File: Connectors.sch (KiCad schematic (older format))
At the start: 1 part, among them J1 USB

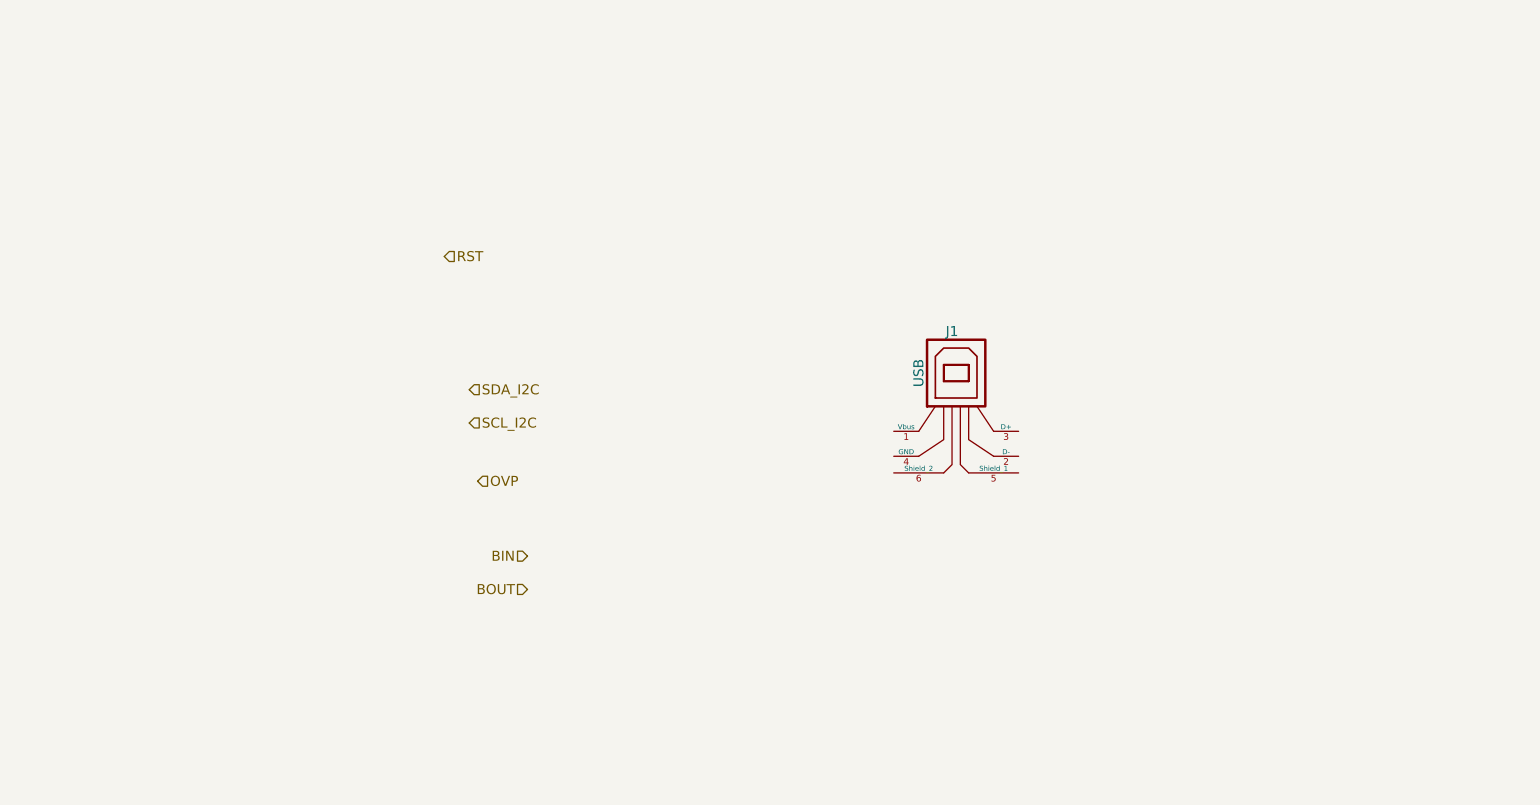
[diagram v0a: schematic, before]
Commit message: Started placing components
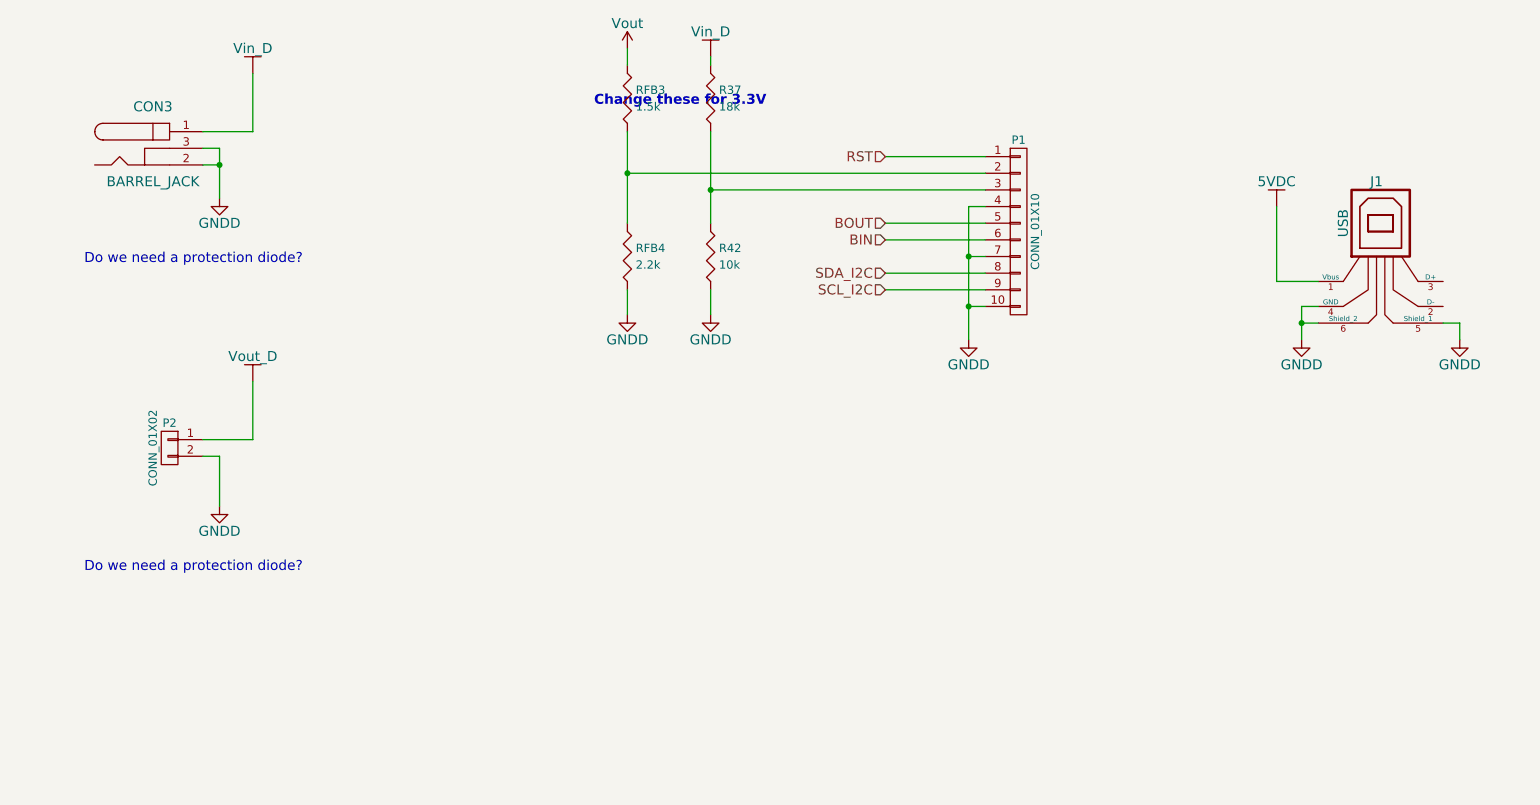
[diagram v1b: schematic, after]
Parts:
- added CON3: BARREL_JACK, Connect:BARREL_JACK, symbol BARREL_JACK
- added P1: CONN_01X10, Socket_Strips:Socket_Strip_Straight_1x10, symbol CONN_01X10
- added P2: CONN_01X02, Socket_Strips:Socket_Strip_Straight_1x02, symbol CONN_01X02
- added R37: 18k, Resistors_SMD:R_0805_HandSoldering, symbol Rv
- added R42: 10k, Resistors_SMD:R_0805_HandSoldering, symbol Rv
- added RFB3: 1.5k, Resistors_SMD:R_0805_HandSoldering, symbol Rv
- added RFB4: 2.2k, Resistors_SMD:R_0805_HandSoldering, symbol Rv
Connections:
- net BIN: now also P1.6 (P6)
- net BOUT: now also P1.5 (P5)
- net RST: now also P1.1 (P1)
- net SCL_I2C: now also P1.9 (P9)
- net SDA_I2C: now also P1.8 (P8)
- net 5VDC: now reaches J1.1 (Vbus)
- net GNDD: now reaches J1.4 (GND)
- net GNDD: now also J1.5 (Shield_1), J1.6 (Shield_2), CON3.2, CON3.3, P1.10 (P10), P1.4 (P4), P1.7 (P7), P2.2 (P2), R42.2, RFB4.2
- new net: P1.3 (P3), R37.2, R42.1
- new net: P1.2 (P2), RFB3.2, RFB4.1
- new net Vin_D: CON3.1, R37.1
- new net Vout: RFB3.1
- new net Vout_D: P2.1 (P1)
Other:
- note added: "Change these for 3.3V"
- note added: "Do we need a protection diode?\n"
- moved on the sheet: J1

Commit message: still trying to get initial placements done.  Still need to fine-tune
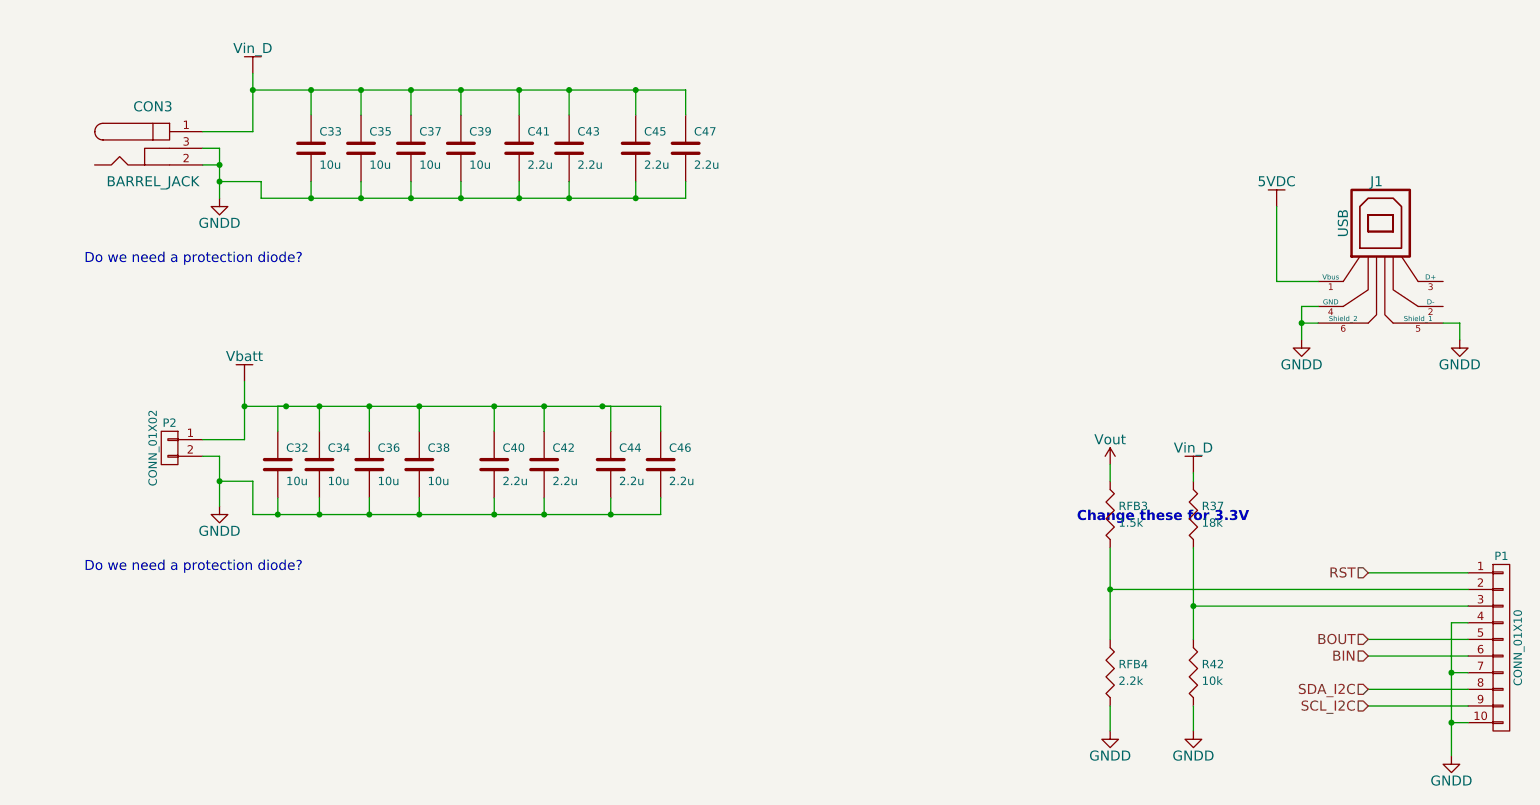
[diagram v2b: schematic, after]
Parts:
- added C32, C33, C34, C35, C36, C37, C38, C39: 10u, Capacitors_SMD:C_0603_HandSoldering, symbol C
- added C40, C41, C42, C43, C44, C45, C46, C47: 2.2u, Capacitors_SMD:C_0603_HandSoldering, symbol C
- R37, R42, RFB3, RFB4: footprint Resistors_SMD:R_0805_HandSoldering -> Resistors_SMD:R_0603_HandSoldering
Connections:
- net GNDD: now also C32.2, C33.2, C34.2, C35.2, C36.2, C37.2, C38.2, C39.2, C40.2, C41.2, C42.2, C43.2, C44.2, C45.2, C46.2, C47.2
- net Vin_D: now also C33.1, C35.1, C37.1, C39.1, C41.1, C43.1, C45.1, C47.1
- net Vout_D renamed Vbatt
- net Vbatt: now also C32.1, C34.1, C36.1, C38.1, C40.1, C42.1, C44.1, C46.1
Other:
- moved on the sheet: P1, R37, R42, RFB3, RFB4

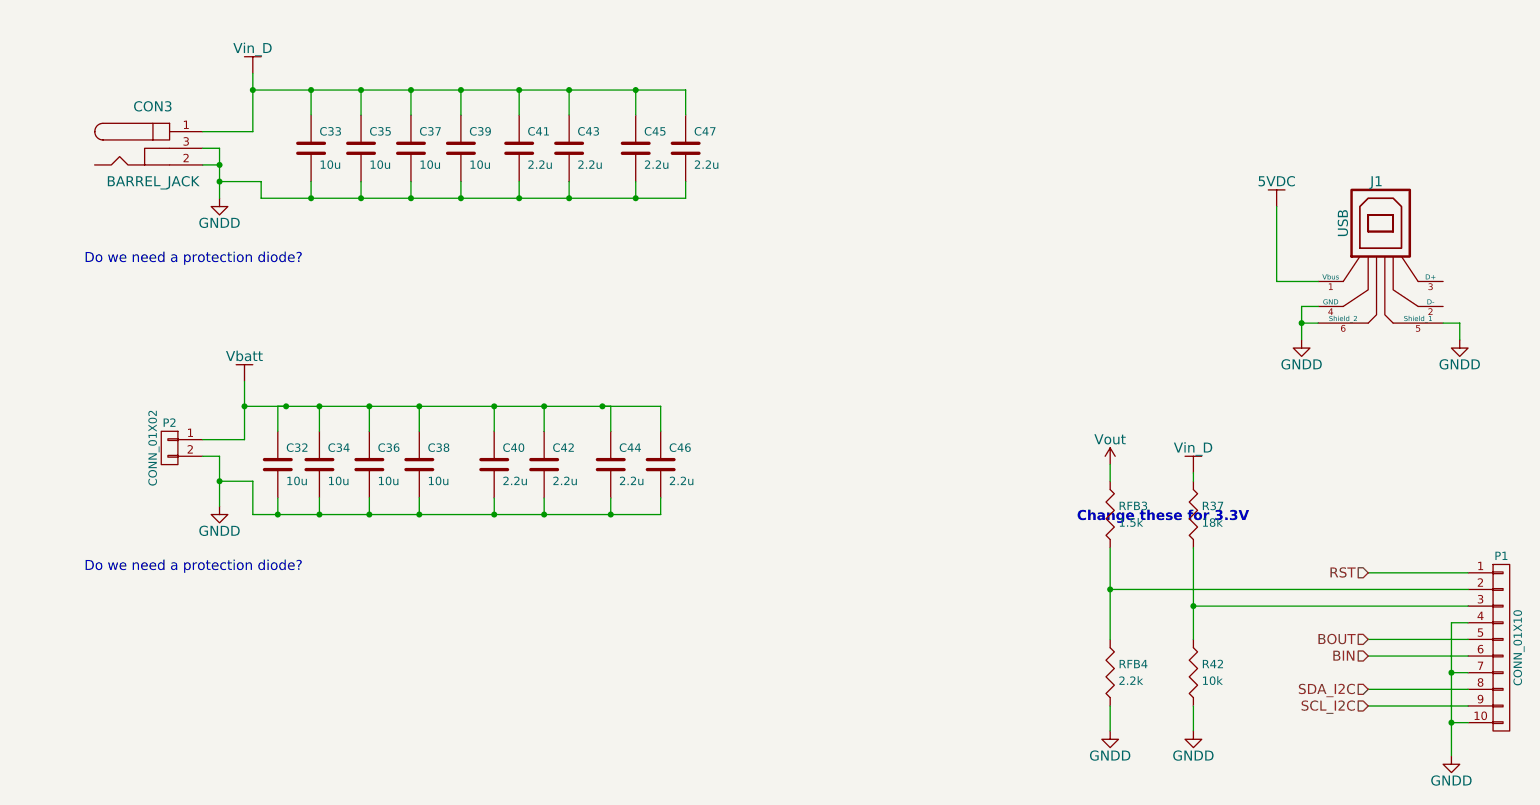
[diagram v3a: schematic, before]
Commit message: Routing done, prepping for DRC
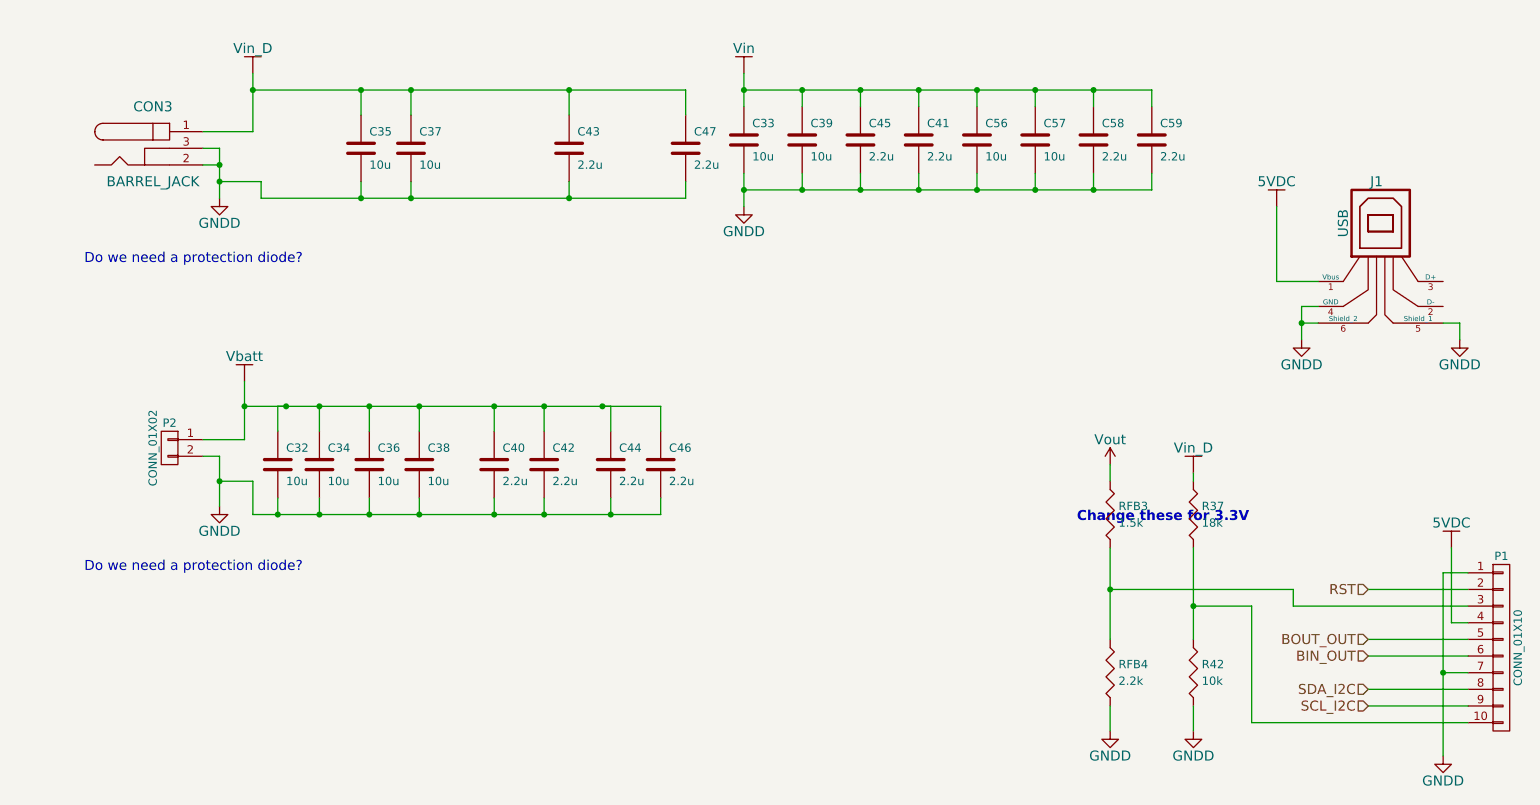
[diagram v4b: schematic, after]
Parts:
- added C56, C57: 10u, Capacitors_SMD:C_0603_HandSoldering, symbol C
- added C58, C59: 2.2u, Capacitors_SMD:C_0603_HandSoldering, symbol C
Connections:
- net 5VDC: now also P1.4 (P4)
- net GNDD: now also P1.1 (P1), C56.2, C57.2, C58.2, C59.2; no longer P1.10 (P10), P1.4 (P4)
- net RST: now also P1.2 (P2); no longer P1.1 (P1)
- net Vin_D: no longer C33.1, C39.1, C41.1, C45.1
- net at R37.2, R42.1: now also P1.10 (P10); no longer P1.3 (P3)
- net at RFB3.2, RFB4.1: now also P1.3 (P3); no longer P1.2 (P2)
- net BIN renamed BIN_OUT
- net BOUT renamed BOUT_OUT
- new net Vin: C33.1, C39.1, C41.1, C45.1, C56.1, C57.1, C58.1, C59.1
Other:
- moved on the sheet: C33, C39, C41, C45

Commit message: Cleared all DRC errors.
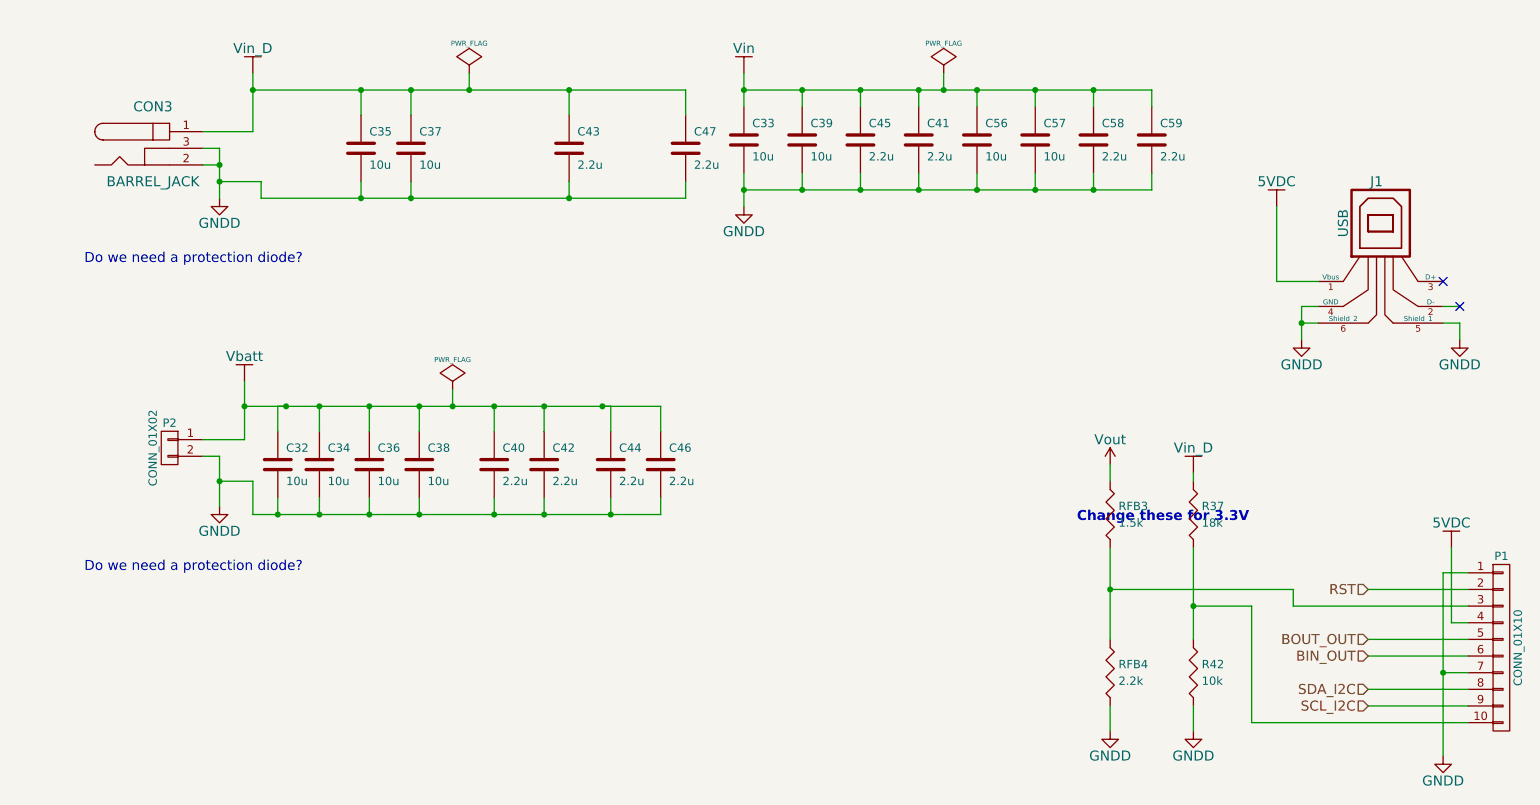
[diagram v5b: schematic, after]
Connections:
- no-connect marks 0 -> 2
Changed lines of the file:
@@
 Do we need a protection diode?\n
 $Comp
-L GNDD #PWR057
+L GNDD #PWR059
 U 1 1 54FDA29A
 P 2200 3550
-F 0 "#PWR057" H 2200 3300 60  0001 C CNN
+F 0 "#PWR059" H 2200 3300 60  0001 C CNN
 F 1 "GNDD" H 2200 3400 60  0000 C CNN
 F 2 "" H 2200 3550 60  0000 C CNN
@@
 $EndComp
 $Comp
-L Vin_D #PWR058
+L Vin_D #PWR060
 U 1 1 54FDA2A9
 P 2400 950
-F 0 "#PWR058" H 2400 800 60  0001 C CNN
+F 0 "#PWR060" H 2400 800 60  0001 C CNN
 F 1 "Vin_D" H 2400 1100 60  0000 C CNN
 F 2 "" H 2400 950 60  0000 C CNN
@@
 Do we need a protection diode?\n
 $Comp
-L GNDD #PWR059
+L GNDD #PWR061
 U 1 1 54FDA2B5
 P 2200 1700
-F 0 "#PWR059" H 2200 1450 60  0001 C CNN
+F 0 "#PWR061" H 2200 1450 60  0001 C CNN
 F 1 "GNDD" H 2200 1550 60  0000 C CNN
 F 2 "" H 2200 1700 60  0000 C CNN
@@
 $EndComp
 $Comp
-L GNDD #PWR060
+L GNDD #PWR062
 U 1 1 54FDAC0A
 P 8050 4900
-F 0 "#PWR060" H 8050 4650 60  0001 C CNN
+F 0 "#PWR062" H 8050 4650 60  0001 C CNN
 F 1 "GNDD" H 8050 4750 60  0000 C CNN
 F 2 "" H 8050 4900 60  0000 C CNN
@@
 $EndComp
 $Comp
-L Vin_D #PWR061
+L Vin_D #PWR063
 U 1 1 54FDAC12
 P 8050 3350
-F 0 "#PWR061" H 8050 3200 60  0001 C CNN
+F 0 "#PWR063" H 8050 3200 60  0001 C CNN
 F 1 "Vin_D" H 8050 3500 60  0000 C CNN
 F 2 "" H 8050 3350 60  0000 C CNN
@@
 $EndComp
 $Comp
-L GNDD #PWR062
+L GNDD #PWR064
 U 1 1 54FDAEB2
 P 7550 4900
-F 0 "#PWR062" H 7550 4650 60  0001 C CNN
+F 0 "#PWR064" H 7550 4650 60  0001 C CNN
 F 1 "GNDD" H 7550 4750 60  0000 C CNN
 F 2 "" H 7550 4900 60  0000 C CNN
@@
 $EndComp
 $Comp
-L Vout #PWR063
+L Vout #PWR065
 U 1 1 54FDAEB9
 P 7550 3300
-F 0 "#PWR063" H 7550 3150 60  0001 C CNN
+F 0 "#PWR065" H 7550 3150 60  0001 C CNN
 F 1 "Vout" H 7550 3450 60  0000 C CNN
 F 2 "" H 7550 3300 60  0000 C CNN
@@
 $EndComp
 $Comp
-L GNDD #PWR064
+L GNDD #PWR066
 U 1 1 54FDAF91
 P 9550 5050
-F 0 "#PWR064" H 9550 4800 60  0001 C CNN
+F 0 "#PWR066" H 9550 4800 60  0001 C CNN
 F 1 "GNDD" H 9550 4900 60  0000 C CNN
 F 2 "" H 9550 5050 60  0000 C CNN
@@
 $EndComp
 $Comp
-L GNDD #PWR065
+L GNDD #PWR067
 U 1 1 54FDB331
 P 8700 2550
-F 0 "#PWR065" H 8700 2300 60  0001 C CNN
+F 0 "#PWR067" H 8700 2300 60  0001 C CNN
 F 1 "GNDD" H 8700 2400 60  0000 C CNN
 F 2 "" H 8700 2550 60  0000 C CNN
@@
 $EndComp
 $Comp
-L 5VDC #PWR066
+L 5VDC #PWR068
 U 1 1 54FDB3B7
 P 8550 1750
-F 0 "#PWR066" H 8550 1600 60  0001 C CNN
+F 0 "#PWR068" H 8550 1600 60  0001 C CNN
 F 1 "5VDC" H 8550 1900 60  0000 C CNN
 F 2 "" H 8550 1750 60  0000 C CNN
@@
 $EndComp
 $Comp
-L GNDD #PWR067
+L GNDD #PWR069
 U 1 1 54FDB422
 P 9650 2550
-F 0 "#PWR067" H 9650 2300 60  0001 C CNN
+F 0 "#PWR069" H 9650 2300 60  0001 C CNN
 F 1 "GNDD" H 9650 2400 60  0000 C CNN
 F 2 "" H 9650 2550 60  0000 C CNN
@@
 $EndComp
 $Comp
-L Vbatt #PWR068
+L Vbatt #PWR070
 U 1 1 54FF753E
 P 2350 2800
-F 0 "#PWR068" H 2350 2650 60  0001 C CNN
+F 0 "#PWR070" H 2350 2650 60  0001 C CNN
 F 1 "Vbatt" H 2350 2950 60  0000 C CNN
 F 2 "" H 2350 2800 60  0000 C CNN
@@
 $EndComp
 $Comp
-L 5VDC #PWR069
+L 5VDC #PWR071
 U 1 1 55020822
 P 9600 3800
-F 0 "#PWR069" H 9600 3650 60  0001 C CNN
+F 0 "#PWR071" H 9600 3650 60  0001 C CNN
 F 1 "5VDC" H 9600 3950 60  0000 C CNN
 F 2 "" H 9600 3800 60  0000 C CNN
@@
 $EndComp
 $Comp
-L GNDD #PWR070
+L GNDD #PWR072
 U 1 1 550228CF
 P 5350 1750
-F 0 "#PWR070" H 5350 1500 60  0001 C CNN
+F 0 "#PWR072" H 5350 1500 60  0001 C CNN
 F 1 "GNDD" H 5350 1600 60  0000 C CNN
 F 2 "" H 5350 1750 60  0000 C CNN
@@
 $EndComp
 $Comp
-L Vin #PWR071
+L Vin #PWR073
 U 1 1 55022913
 P 5350 950
-F 0 "#PWR071" H 5350 800 60  0001 C CNN
+F 0 "#PWR073" H 5350 800 60  0001 C CNN
 F 1 "Vin" H 5350 1100 60  0000 C CNN
 F 2 "" H 5350 950 60  0000 C CNN
@@
 Wire Wire Line
 	5350 1050 7800 1050
+NoConn ~ 9550 2200
+NoConn ~ 9650 2350
+Wire Wire Line
+	9650 2350 9550 2350
+$Comp
+L PWR_FLAG #FLG074
+U 1 1 55031A54
+P 3600 2850
+F 0 "#FLG074" H 3600 2945 30  0001 C CNN
+F 1 "PWR_FLAG" H 3600 3030 30  0000 C CNN
+F 2 "" H 3600 2850 60  0000 C CNN
+F 3 "" H 3600 2850 60  0000 C CNN
+	1    3600 2850
+	1    0    0    -1
+$EndComp
+$Comp
+L PWR_FLAG #FLG075
+U 1 1 55031AA0
+P 3700 950
+F 0 "#FLG075" H 3700 1045 30  0001 C CNN
+F 1 "PWR_FLAG" H 3700 1130 30  0000 C CNN
+F 2 "" H 3700 950 60  0000 C CNN
+F 3 "" H 3700 950 60  0000 C CNN
+	1    3700 950
+	1    0    0    -1
+$EndComp
+$Comp
+L PWR_FLAG #FLG076
+U 1 1 55031ACE
+P 6550 950
+F 0 "#FLG076" H 6550 1045 30  0001 C CNN
+F 1 "PWR_FLAG" H 6550 1130 30  0000 C CNN
+F 2 "" H 6550 950 60  0000 C CNN
+F 3 "" H 6550 950 60  0000 C CNN
+	1    6550 950
+	1    0    0    -1
+$EndComp
+Wire Wire Line
+	3700 1050 3700 950
+Connection ~ 3700 1050
+Wire Wire Line
+	3600 2950 3600 2850
+Connection ~ 3600 2950
+Wire Wire Line
+	6550 1050 6550 950
+Connection ~ 6550 1050
 $EndSCHEMATC
